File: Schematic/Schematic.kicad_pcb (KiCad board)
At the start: 2 copper layers, 115.1 x 171.2 mm, 102 parts, among them J1 Conn_02x08_Odd_Even, J10 Conn_01x03_Pin, J11 Conn_01x03_Pin, J12 Conn_01x03_Pin, J13 Conn_01x03_Pin, J14 Conn_01x03_Pin, J15 Conn_01x03_Pin, J16 Conn_01x03_Pin, J17 Conn_01x03_Pin, J2 Conn_01x08, J3 Conn_01x04_Pin, J4 Conn_02x01, J5 Conn_02x05_Odd_Even, J6 Conn_01x03_Pin, J7 Conn_01x03_Pin, J8 Conn_01x03_Pin, J9 Conn_01x03_Pin, SW1 SW_Push, U1 74LS08, U2 STM32F091RCT6, U3 LM386, U4 LM2678S-12, U5 LD1117S33TR_SOT223, U6 MAX7375AXR805

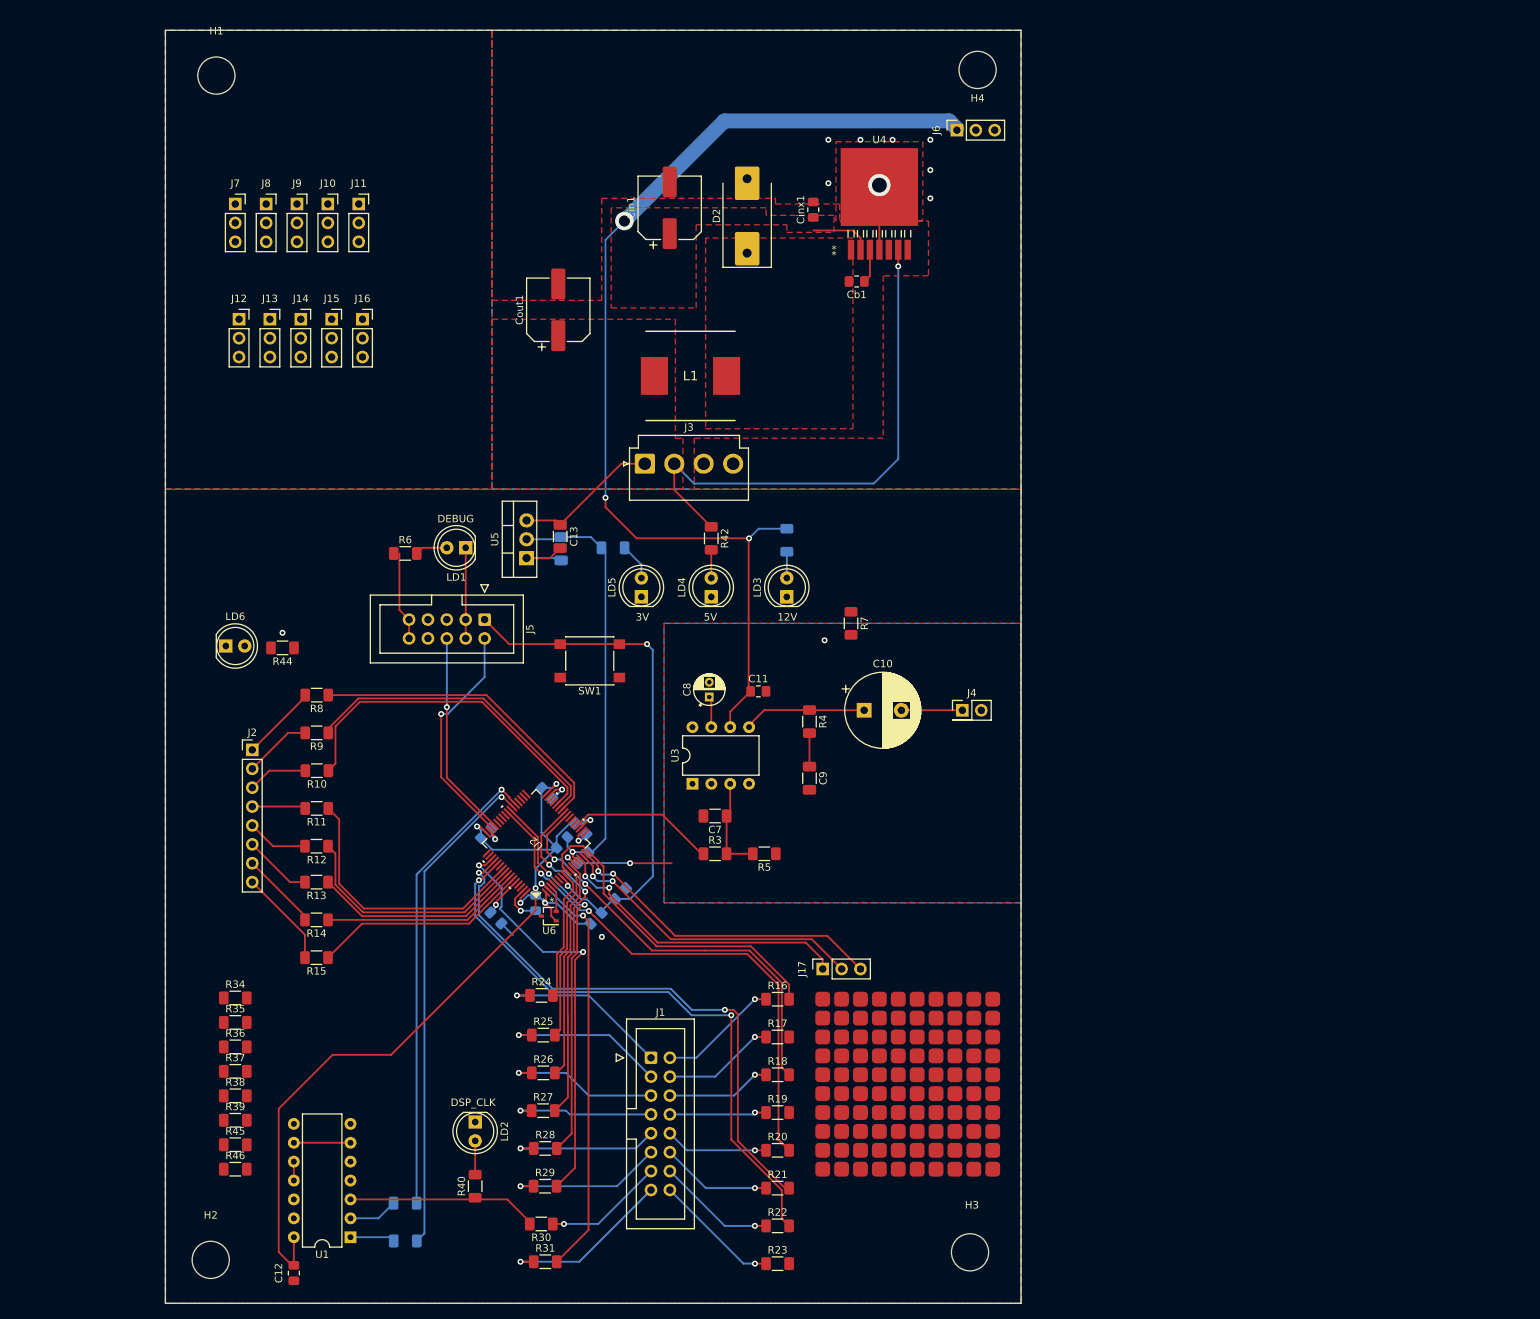
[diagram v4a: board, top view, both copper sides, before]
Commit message: Added sensors. Fixed other stuff.
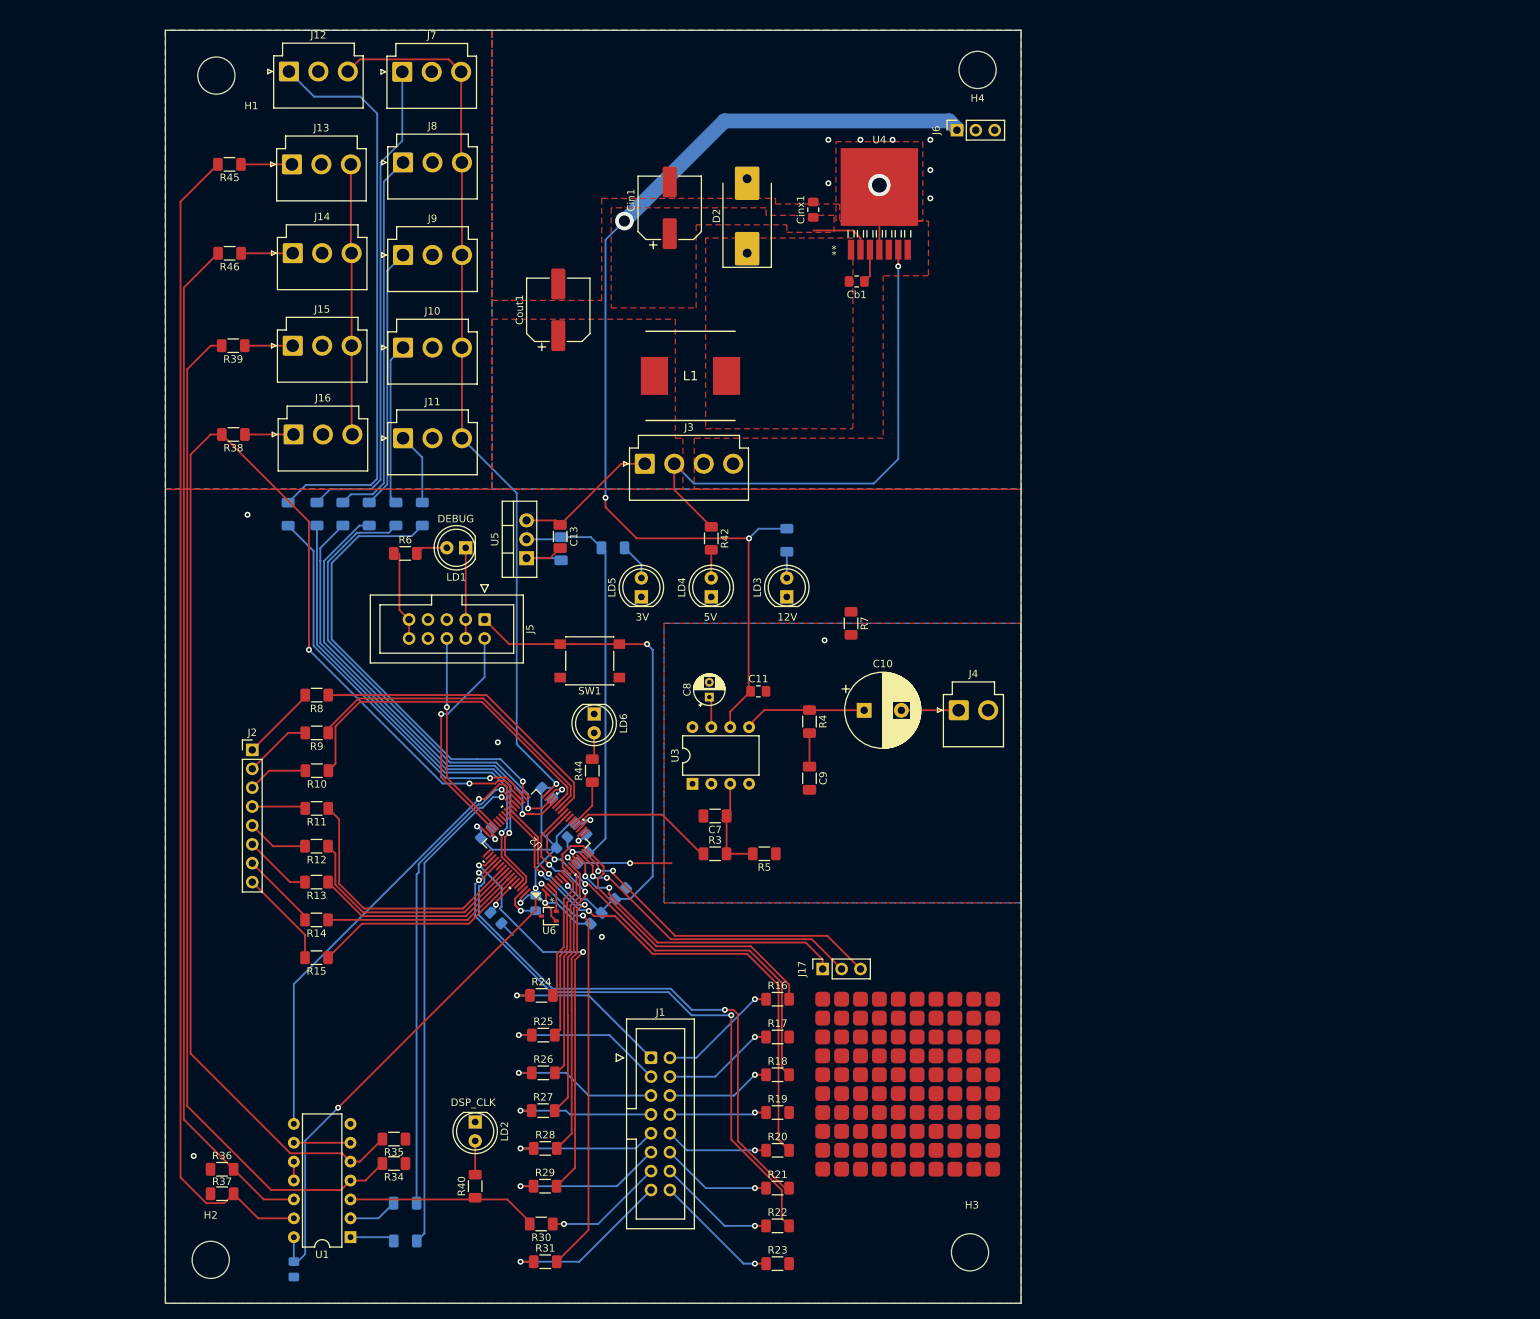
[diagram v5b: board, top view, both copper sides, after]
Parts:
- added R47: 1k, Resistor_SMD:R_1206_3216Metric_Pad1.30x1.75mm_HandSolder, B.Cu at (76.5, 89.4)
- added R48: 1k, Resistor_SMD:R_1206_3216Metric_Pad1.30x1.75mm_HandSolder, B.Cu at (80.0, 89.4)
- added R49: 1k, Resistor_SMD:R_1206_3216Metric_Pad1.30x1.75mm_HandSolder, B.Cu at (83.5, 89.4)
- added R50: 1k, Resistor_SMD:R_1206_3216Metric_Pad1.30x1.75mm_HandSolder, B.Cu at (87.1, 89.4)
- added R51: 1k, Resistor_SMD:R_1206_3216Metric_Pad1.30x1.75mm_HandSolder, B.Cu at (90.7, 89.4)
- added R52: 1k, Resistor_SMD:R_1206_3216Metric_Pad1.30x1.75mm_HandSolder, B.Cu at (72.6, 89.5)
- C12: moved to B.Cu
- J10, J11, J12, J13, J14, J15, J16, J7, J8, J9: footprint Connector_PinSocket_2.54mm:PinSocket_1x03_P2.54mm_Vertical -> Connector_JST:JST_VH_B3P-VH_1x03_P3.96mm_Vertical
- J4: footprint Connector_PinHeader_2.54mm:PinHeader_2x01_P2.54mm_Vertical -> Connector_JST:JST_VH_B2P-VH-B_1x02_P3.96mm_Vertical
- moved R45 131.8 mm to (64.7, 42.4), turned to 180 degrees
- moved R46 123.2 mm to (64.8, 54.4), turned to 180 degrees
- moved R39 104.2 mm to (65.3, 66.8), turned to 180 degrees
- moved R38 88.9 mm to (65.3, 78.7), turned to 180 degrees
- moved LD6 50.4 mm to (113.8, 116.3), turned to -90 degrees
- moved R44 44.8 mm to (113.5, 124.0), turned to 90 degrees
- moved J12 34.0 mm to (72.7, 29.9)
- moved J11 32.1 mm to (88.1, 79.2)
- moved R34 30.8 mm to (86.9, 176.8), turned to 180 degrees
- moved J7 28.6 mm to (88.0, 30.0)
- moved R35 26.5 mm to (86.9, 173.5), turned to 180 degrees
- moved J10 21.8 mm to (88.1, 67.1)
- moved J13 21.0 mm to (73.2, 42.4)
- moved J8 19.2 mm to (88.1, 42.2)
- moved J16 18.1 mm to (73.4, 78.7)
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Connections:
- net VA renamed Vin
- J10 pad 1: unconnected-(J10-Pin_1-Pad1) -> Net-(J10-Pin_1)
- J10 pad 2: unconnected-(J10-Pin_2-Pad2) -> GND
- J10 pad 3: unconnected-(J10-Pin_3-Pad3) -> +3V0
- J11 pad 1: unconnected-(J11-Pin_1-Pad1) -> Net-(J11-Pin_1)
- J11 pad 2: unconnected-(J11-Pin_2-Pad2) -> GND
- J11 pad 3: unconnected-(J11-Pin_3-Pad3) -> +3V0
- J12 pad 1: unconnected-(J12-Pin_1-Pad1) -> Net-(J12-Pin_1)
- J12 pad 2: unconnected-(J12-Pin_2-Pad2) -> GND
- J12 pad 3: unconnected-(J12-Pin_3-Pad3) -> +3V0
- J13 pad 1: unconnected-(J13-Pin_1-Pad1) -> Net-(J13-Pin_1)
- J13 pad 2: unconnected-(J13-Pin_2-Pad2) -> GND
- J13 pad 3: unconnected-(J13-Pin_3-Pad3) -> Net-(J13-Pin_3)
- J14 pad 1: unconnected-(J14-Pin_1-Pad1) -> Net-(J14-Pin_1)
- J14 pad 2: unconnected-(J14-Pin_2-Pad2) -> GND
- J14 pad 3: unconnected-(J14-Pin_3-Pad3) -> Net-(J13-Pin_3)
- J15 pad 1: unconnected-(J15-Pin_1-Pad1) -> Net-(J15-Pin_1)
- J15 pad 2: unconnected-(J15-Pin_2-Pad2) -> GND
- J15 pad 3: unconnected-(J15-Pin_3-Pad3) -> Net-(J13-Pin_3)
- J16 pad 1: unconnected-(J16-Pin_1-Pad1) -> Net-(J16-Pin_1)
- J16 pad 2: unconnected-(J16-Pin_2-Pad2) -> GND
- J16 pad 3: unconnected-(J16-Pin_3-Pad3) -> Net-(J13-Pin_3)
- J7 pad 1: unconnected-(J7-Pin_1-Pad1) -> Net-(J7-Pin_1)
- J7 pad 2: unconnected-(J7-Pin_2-Pad2) -> GND
- J7 pad 3: unconnected-(J7-Pin_3-Pad3) -> +3V0
- J8 pad 1: unconnected-(J8-Pin_1-Pad1) -> Net-(J8-Pin_1)
- J8 pad 2: unconnected-(J8-Pin_2-Pad2) -> GND
- J8 pad 3: unconnected-(J8-Pin_3-Pad3) -> +3V0
- J9 pad 1: unconnected-(J9-Pin_1-Pad1) -> Net-(J9-Pin_1)
- J9 pad 2: unconnected-(J9-Pin_2-Pad2) -> GND
- J9 pad 3: unconnected-(J9-Pin_3-Pad3) -> +3V0
- R35 pad 2: Net-(R35-Pad2) -> PB14
- R38 pad 1: unconnected-(R38-Pad1) -> Net-(J16-Pin_1)
- R38 pad 2: Net-(R35-Pad2) -> PB14
- R39 pad 1: unconnected-(R39-Pad1) -> Net-(J15-Pin_1)
- R45 pad 1: unconnected-(R45-Pad1) -> Net-(J13-Pin_1)
- R46 pad 1: unconnected-(R46-Pad1) -> Net-(J14-Pin_1)
- U1 pad 5: Net-(R35-Pad2) -> PB14
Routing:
- net PB14: track 0.00 -> 190.1 mm, vias 0 -> 2
- net Net-(R37-Pad2): track 0.00 -> 156.9 mm
- net Net-(R36-Pad2): track 0.00 -> 137.6 mm
- net Net-(R34-Pad2): track 0.00 -> 137.4 mm
- net +3V0: track 136.1 -> 246.3 mm, vias 6 -> 7
- net Net-(J12-Pin_1): track 0.00 -> 76.6 mm
- net PB9: track 0.00 -> 66.0 mm, vias 0 -> 1
- net Net-(J7-Pin_1): track 0.00 -> 65.9 mm
- net PB8: track 0.00 -> 64.3 mm, vias 0 -> 1
- net PB11: track 0.00 -> 62.8 mm, vias 0 -> 1
- net PB10: track 0.00 -> 61.7 mm, vias 0 -> 1
- net PB15: track 0.00 -> 61.4 mm, vias 0 -> 1
- net PB12: track 0.00 -> 60.1 mm, vias 0 -> 1
- net PB13: track 0.00 -> 54.5 mm, vias 0 -> 1
- net Net-(J8-Pin_1): track 0.00 -> 50.8 mm
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
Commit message: Mostly finallized PCB
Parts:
- added J18: LASER, Connector_JST:JST_VH_B2P-VH-B_1x02_P3.96mm_Vertical, F.Cu at (62.3, 138.4)
- added J19: LDR, Connector_JST:JST_VH_B2P-VH-B_1x02_P3.96mm_Vertical, F.Cu at (62.2, 122.4)
- added J20: WS2812B_DATA, Connector_JST:JST_VH_B2P-VH-B_1x02_P3.96mm_Vertical, F.Cu at (100.9, 115.8)
- added J21: WS2812B_PWR, Connector_JST:JST_VH_B2P-VH-B_1x02_P3.96mm_Vertical, F.Cu at (149.6, 90.9)
- added R53: 100, Resistor_SMD:R_1206_3216Metric_Pad1.30x1.75mm_HandSolder, F.Cu at (64.0, 130.3)
- added R54: 10k, Resistor_SMD:R_1206_3216Metric_Pad1.30x1.75mm_HandSolder, F.Cu at (71.4, 124.0)
- added R55: 2k, Resistor_SMD:R_1206_3216Metric_Pad1.30x1.75mm_HandSolder, B.Cu at (91.9, 35.3)
- added R56: 1k, Resistor_SMD:R_1206_3216Metric_Pad1.30x1.75mm_HandSolder, F.Cu at (62.0, 95.8)
- added R57: 1k, Resistor_SMD:R_1206_3216Metric_Pad1.30x1.75mm_HandSolder, F.Cu at (62.0, 89.4)
- added R58: 2k, Resistor_SMD:R_1206_3216Metric_Pad1.30x1.75mm_HandSolder, B.Cu at (91.9, 47.5)
- added R59: 2k, Resistor_SMD:R_1206_3216Metric_Pad1.30x1.75mm_HandSolder, B.Cu at (91.9, 59.7)
- added R60: 2k, Resistor_SMD:R_1206_3216Metric_Pad1.30x1.75mm_HandSolder, B.Cu at (91.9, 72.1)
- added R61: 2k, Resistor_SMD:R_1206_3216Metric_Pad1.30x1.75mm_HandSolder, B.Cu at (91.9, 84.1)
- added R62: 2k, Resistor_SMD:R_1206_3216Metric_Pad1.30x1.75mm_HandSolder, B.Cu at (77.2, 59.7)
- added R63: 2k, Resistor_SMD:R_1206_3216Metric_Pad1.30x1.75mm_HandSolder, B.Cu at (77.2, 47.8)
- added R64: 2k, Resistor_SMD:R_1206_3216Metric_Pad1.30x1.75mm_HandSolder, B.Cu at (77.2, 84.1)
- added R65: 2k, Resistor_SMD:R_1206_3216Metric_Pad1.30x1.75mm_HandSolder, B.Cu at (77.2, 71.9)
- added R66: 2k, Resistor_SMD:R_1206_3216Metric_Pad1.30x1.75mm_HandSolder, B.Cu at (76.7, 35.1)
- added R67: 7.5k, LED_SMD:LED_1206_3216Metric_Pad1.42x1.75mm_HandSolder, F.Cu at (110.5, 115.4)
- added R68: 3k, LED_SMD:LED_1206_3216Metric_Pad1.42x1.75mm_HandSolder, F.Cu at (113.0, 123.4)
- added RV1: R_Potentiometer, Potentiometer_THT:Potentiometer_Vishay_148-149_Single_Vertical, F.Cu at (81.9, 106.9)
- added TP1: GND, TestPoint:TestPoint_THTPad_D2.0mm_Drill1.0mm, F.Cu at (143.5, 87.9)
- added TP2: 5V, TestPoint:TestPoint_THTPad_D2.0mm_Drill1.0mm, F.Cu at (112.0, 88.6)
- added TP3: 12V, TestPoint:TestPoint_THTPad_D2.0mm_Drill1.0mm, F.Cu at (119.6, 92.2)
- added TP4: 3V, TestPoint:TestPoint_THTPad_D2.0mm_Drill1.0mm, F.Cu at (111.0, 100.1)
- added U7: LM358, Package_DIP:DIP-8_W7.62mm, F.Cu at (73.4, 98.5)
- C12: moved to F.Cu
- J1: value Conn_02x08_Odd_Even -> HUB75_DATA
- J2: value Conn_01x08 -> KEYPAD
- J3: value Conn_01x04_Pin -> HUB75_PWR
- J4: value Conn_02x01 -> AUDIO_OUT
- J5: value Conn_02x05_Odd_Even -> DEBUG_HEADER
- R38, R39, R45, R46: moved to B.Cu
- SW1: value SW_Push -> RESET
- moved R47 55.3 mm to (87.9, 35.3)
- moved R52 54.4 mm to (72.6, 35.1)
- moved R48 42.7 mm to (88.1, 47.5)
- moved R49 30.1 mm to (88.1, 59.7)
- moved R50 17.3 mm to (88.1, 72.1)
- moved R12 10.9 mm to (87.4, 134.1)
- moved R13 10.9 mm to (87.4, 138.9)
- moved R14 10.9 mm to (87.4, 144.0)
- moved R15 10.9 mm to (87.4, 149.1)
- moved J2 10.9 mm to (78.7, 121.2)
- moved R10 10.9 mm to (87.4, 124.0)
- moved R11 10.9 mm to (87.4, 129.0)
- moved R8 10.9 mm to (87.4, 113.8)
- moved R9 10.9 mm to (87.4, 118.9)
- moved R45 9.96 mm to (73.2, 47.8), turned to -90 degrees
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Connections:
- J10 pad 3: +3V0 -> +5V
- J11 pad 3: +3V0 -> +5V
- J12 pad 3: +3V0 -> +5V
- J13 pad 3: Net-(J13-Pin_3) -> +5V
- J14 pad 3: Net-(J13-Pin_3) -> +5V
- J15 pad 3: Net-(J13-Pin_3) -> +5V
- J16 pad 3: Net-(J13-Pin_3) -> +5V
- J7 pad 3: +3V0 -> +5V
- J8 pad 3: +3V0 -> +5V
- J9 pad 3: +3V0 -> +5V
- R35 pad 2: PB14 -> Net-(R35-Pad2)
- R38 pad 2: PB14 -> Net-(R35-Pad2)
- U1 pad 5: PB14 -> Net-(R35-Pad2)
- U2 pad 23: unconnected-(U2-PA7-Pad23) -> PA7
- U2 pad 3: Net-(U2-PC14-OSC32_IN) -> unconnected-(U2-PC14-OSC32_IN-Pad3)
- U2 pad 45: /microprocessor/SWCLK_IN -> unconnected-(U2-PA12-Pad45)
- U2 pad 49: unconnected-(U2-PA14-Pad49) -> /microprocessor/SWCLK_IN
- U2 pad 5: unconnected-(U2-PF0-OSC_IN-Pad5) -> Net-(U2-PF0-OSC_IN)
- U6 pad 2: Net-(U2-PC14-OSC32_IN) -> Net-(U2-PF0-OSC_IN)
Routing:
- net +5V: track 90.8 -> 394.2 mm
- net PB14: track 190.1 -> 52.0 mm, vias 2 -> 1
- net Net-(R35-Pad2): track 0.00 -> 126.2 mm
- net +3V0: track 246.3 -> 128.1 mm, vias 7 -> 6
- net Net-(J12-Pin_1): track 76.6 -> 3.11 mm
- net Net-(J7-Pin_1): track 65.9 -> 3.83 mm
- net PB13: track 54.5 -> 111.2 mm
- net PB8: track 64.3 -> 119.1 mm
- net Net-(J8-Pin_1): track 50.8 -> 3.80 mm
- net PB9: track 66.0 -> 107.0 mm
- net Net-(J13-Pin_3): track 36.4 -> 0.00 mm
- net Net-(J19-Pin_2): track 0.00 -> 32.5 mm
- net Net-(J9-Pin_1): track 35.2 -> 3.58 mm
- net PB10: track 61.7 -> 88.4 mm
- net Net-(U7A-+): track 0.00 -> 19.5 mm
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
